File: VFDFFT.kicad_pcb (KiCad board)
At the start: 2 copper layers, 261 parts, among them J1 USB_C_Receptacle_USB2.0, J10 Conn_01x02_Pin, J11 Conn_01x02_Male, J12 Conn_01x02_Male, J13 Conn_01x02_Male, J2 BATT, J3 FILAMENT+, J4 VFD_SIG, J5 USB_A, J6 Conn_01x03_Socket, J7 Conn_01x03_Socket, J8 Conn_01x02_Pin, J9 Conn_01x02_Pin, Q1 IRL7486MTRPBF, Q10 AO3400A, Q11 AO3400A, Q12 FS5N10S, Q2 ASDM30DN40E, Q3 ASDM30DN40E, Q4 HSCB2903, Q5 HSCB2903, Q6 AP6800, Q7 FS5N10S, Q8 FS5N10S, Q9 AO3400A, U1 IP2368, U10 TPS61170, U11 TPS61170, U12 W25Q128JVS, U13 TPS62170DSG, U14 LM358, U15 LM324, U16 LM3478, U17 LM2738, U18 LTC1446, U2 78L05_SOT23, U3 TPS40305, U4 LM3478, U5 LM3478, U6 STM32F446VETx, U7 AP6181, U8 HDC1080, U9 OPT3001DNPR, X1 SX1M32.768KM10F30TNN, Y1 26M, Y2 24M

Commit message: file sync
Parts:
- Y1: value 26M -> WTL3M45404LZ; footprint Crystal:Crystal_SMD_2016-4Pin_2.0x1.6mm -> Crystal:Crystal_SMD_3225-4Pin_3.2x2.5mm
- moved U12 263.9 mm to (-174.3, 77.1)
- moved U10 239.1 mm to (-144.2, 46.5)
- moved D11 238.5 mm to (-148.4, 56.4)
- moved L9 236.9 mm to (-147.3, 28.2)
- moved L7 233.1 mm to (-147.7, 52.9)
- moved C68 229.2 mm to (-148.3, 46.2)
- moved C71 229.2 mm to (-148.3, 49.2)
- moved U9 229.1 mm to (-116.8, -21.2)
- moved R58 227.7 mm to (-177.5, 84.3)
- moved U11 220.6 mm to (-121.5, 27.7)
- moved D12 217.8 mm to (-125.7, 37.6)
- moved L8 213.1 mm to (-125.0, 34.1)
- moved C76 212.1 mm to (-177.5, 81.8)
- moved U8 211.6 mm to (-116.0, -25.3)
- moved C72 210.5 mm to (-125.6, 27.4)
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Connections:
- C10 pad 2: Net-(Q2B-D) -> Net-(Q2A-S)
- C13 pad 2: Net-(Q3B-D) -> Net-(Q3A-S)
- C48 pad 1: Net-(U7-XTAL_IN) -> Net-(C48-Pad1)
- L1 pad 1: Net-(Q2B-D) -> Net-(Q2A-S)
- L1 pad 2: Net-(Q3B-D) -> Net-(Q3A-S)
- Q2 pad 5: Net-(Q2B-D) -> Net-(Q2A-S)
- Q2 pad 7: Net-(Q2A-D)_1 -> Net-(U1-PCIN)
- Q2 pad 8: Net-(Q2A-D) -> Net-(U1-PCIN)
- Q3 pad 5: Net-(Q3B-D) -> Net-(Q3A-S)
- Q3 pad 7: Net-(Q3A-D)_1 -> Net-(U1-PCON)
- Q3 pad 8: Net-(Q3A-D) -> Net-(U1-PCON)
- R10 pad 1: Net-(Q2A-D) -> Net-(U1-PCIN)
- R11 pad 1: Net-(Q2B-D) -> Net-(Q2A-S)
- R12 pad 1: Net-(Q3A-D) -> Net-(U1-PCON)
- R13 pad 1: Net-(Q3A-D) -> Net-(U1-PCON)
- R14 pad 1: Net-(Q3B-D) -> Net-(Q3A-S)
- R42 pad 2: Net-(R42-Pad2) -> Net-(C48-Pad1)
- R9 pad 1: Net-(Q2A-D) -> Net-(U1-PCIN)
- U1 pad 15: Net-(Q2A-D)_1 -> Net-(U1-PCIN)
- U1 pad 18: Net-(Q2B-D) -> Net-(Q2A-S)
- U1 pad 21: Net-(Q3B-D) -> Net-(Q3A-S)
- U1 pad 24: Net-(Q3A-D)_1 -> Net-(U1-PCON)
- Y1 pad 2: Net-(R42-Pad2) -> GND
- Y1 pad 3: (no net) -> Net-(C48-Pad1)
- Y1 pad 4: (no net) -> GND
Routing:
- net GND: track 0.00 -> 133.0 mm, vias 0 -> 171
- net +BATT: track 0.00 -> 130.9 mm, vias 0 -> 17
- net /HLED: track 0.00 -> 79.7 mm, vias 0 -> 7
- net /CC2: track 0.00 -> 67.5 mm, vias 0 -> 2
- net PRI_HI: track 0.00 -> 61.0 mm, vias 0 -> 4
- net /BAT_MODE: track 0.00 -> 59.0 mm, vias 0 -> 6
- net /CC1: track 0.00 -> 57.7 mm, vias 0 -> 6
- net Net-(Q3A-G): track 0.00 -> 37.8 mm, vias 0 -> 2
- net Net-(D7-A2): track 0.00 -> 36.1 mm, vias 0 -> 2
- net Net-(Q3B-G): track 0.00 -> 36.0 mm, vias 0 -> 2
- net Net-(U1-PCON): track 0.00 -> 35.9 mm, vias 0 -> 17
- net /LED3: track 0.00 -> 31.5 mm, vias 0 -> 3
- net Net-(Q3A-S): track 0.00 -> 31.3 mm, vias 0 -> 62
- net /3V3_FB: track 0.00 -> 25.6 mm, vias 0 -> 4
- net +3V3: track 0.00 -> 24.8 mm, vias 0 -> 3
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- added copper zone on B.Cu, net +BATT
- added copper zone on F.Cu, net +BATT
- added copper zone on F.Cu, net /CC1
- added copper zone on F.Cu, net /CC2
- added copper zone on F.Cu, net /VB_S
- added copper zone on B.Cu, net GND
- added copper zone on F.Cu, net GND
- added copper zone on F.Cu, net Net-(F1-Pad1)
- added copper zone on F.Cu, net Net-(Q2A-S)
- added copper zone on B.Cu, net Net-(Q3A-S)
- added copper zone on F.Cu, net Net-(Q4A-D)
- added copper zone on F.Cu, net Net-(Q5A-D)
- added copper zone on B.Cu, net Net-(U1-PCIN)
- added copper zone on B.Cu, net Net-(U1-PCON)
- added copper zone on F.Cu, net VBUS
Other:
- board outline added: 100 x 50 mm
- board text added: "3V3"
- board text added: "ANODE BOOST"
- board text added: "BATTERY CHARGE"
- board text added: "Charging (NO DATA HERE)"
- board text added: "GRID BOOST"
- board text added: "SHELL MOS"
- board text added: "VDD VHP GND"
- board text added: "装不回去了吧"

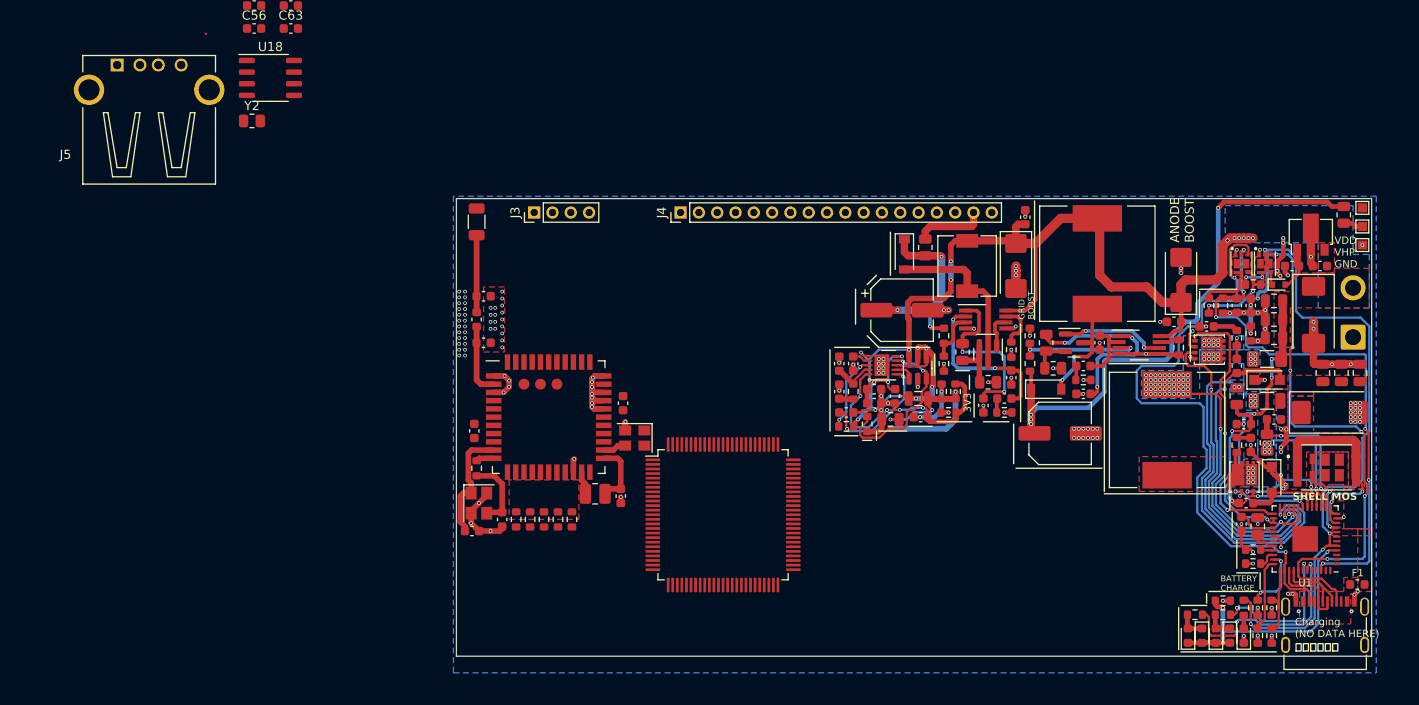
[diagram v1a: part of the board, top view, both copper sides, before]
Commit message: SDIO routing
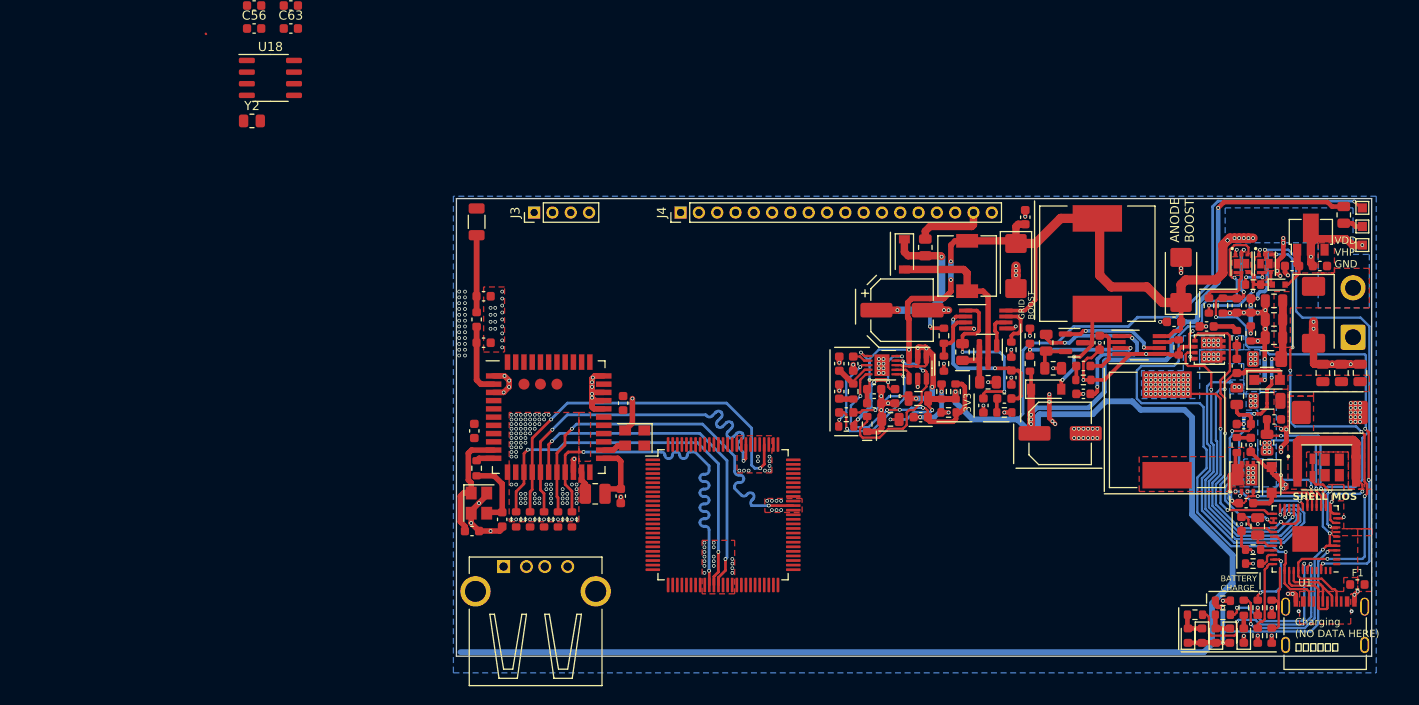
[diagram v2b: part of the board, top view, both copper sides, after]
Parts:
- moved J5 69.2 mm to (49.9, 77.0)
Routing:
- net +3V3: track 24.8 -> 212.8 mm, vias 3 -> 4
- net /WL_D2: track 0.00 -> 42.9 mm, vias 0 -> 2
- net /WL_D3: track 0.00 -> 42.7 mm, vias 0 -> 2
- net /WL_D1: track 0.00 -> 42.5 mm, vias 0 -> 2
- net /WL_D0: track 0.00 -> 42.4 mm, vias 0 -> 2
- net /WL_CMD: track 0.00 -> 41.8 mm, vias 0 -> 2
- net /WL_CLK: track 0.00 -> 38.2 mm, vias 0 -> 2
- net GND: track 133.0 -> 164.9 mm, vias 171 -> 305

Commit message: file sync
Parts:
- added C92: 1uF, Capacitor_SMD:C_0603_1608Metric, F.Cu at (24.0, 59.4)
- added C93: 1uF, Capacitor_SMD:C_0603_1608Metric, F.Cu at (24.0, 61.9)
- added C94: 1uF, Capacitor_SMD:C_0603_1608Metric, F.Cu at (24.0, 64.4)
- added C95: 10uF, Capacitor_SMD:C_0603_1608Metric, F.Cu at (24.0, 66.9)
- added C96: 4.7uF, Capacitor_SMD:C_0603_1608Metric, F.Cu at (-15.1, 65.6)
- added C97: 4.7uF, Capacitor_SMD:C_0603_1608Metric, F.Cu at (-15.1, 68.2)
- added C98: 3.3nF, Capacitor_SMD:C_0603_1608Metric, F.Cu at (109.5, 75.7)
- added J14: AudioJack3_Ground, Footprints:TRRS-PJ-320A, F.Cu at (-9.50, 67.0)
- added J15: USB_C_Receptacle_USB2.0, Footprints:TYPE-C-31-M-31, F.Cu at (114.8, 79.8)
- added R90: 100K, Capacitor_SMD:C_0603_1608Metric, F.Cu at (24.0, 69.5)
- added R91: 100K, Capacitor_SMD:C_0603_1608Metric, F.Cu at (24.0, 72.0)
- added R92: 1K, Resistor_SMD:R_0603_1608Metric, F.Cu at (80.8, 65.8)
- added R93: 1K, Resistor_SMD:R_0603_1608Metric, F.Cu at (109.5, 74.2)
- added R94: 5K1, Resistor_SMD:R_0603_1608Metric, F.Cu at (109.0, 82.3)
- added R95: 5K1, Resistor_SMD:R_0603_1608Metric, F.Cu at (121.7, 77.7)
- added RN2: 22, Resistor_SMD:R_Array_Concave_4x0603, F.Cu at (91.2, 76.2)
- added U19: CH340E, Package_SO:MSOP-10_3x3mm_P0.5mm, F.Cu at (114.3, 74.7)
- U18: value LTC1446 -> ES9023; footprint Package_SO:SO-8_3.9x4.9mm_P1.27mm -> Package_SO:SO-16_3.9x9.9mm_P1.27mm
- moved U12 262.0 mm to (87.6, 81.0), turned to 180 degrees
- moved C76 237.9 mm to (58.6, 111.4)
- moved R58 237.9 mm to (58.6, 114.0)
- moved R43 219.4 mm to (70.4, 81.8), turned to 90 degrees
- moved R44 214.6 mm to (67.8, 79.0), turned to 180 degrees
- moved U8 212.4 mm to (67.4, 81.9)
- moved R49 210.9 mm to (64.5, 82.3), turned to -90 degrees
- moved R47 210.7 mm to (63.0, 82.3), turned to 90 degrees
- moved U9 205.1 mm to (60.3, 82.3)
- moved RN1 187.6 mm to (73.7, 80.0), turned to 90 degrees
- moved R48 182.5 mm to (71.1, 38.4)
- moved C67 179.4 mm to (68.1, 38.4)
- moved U18 56.5 mm to (5.33, 75.2), turned to 90 degrees
- moved C56 18.2 mm to (16.3, 33.5)
- moved C63 18.2 mm to (20.3, 33.5)
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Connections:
- net Net-(J5-D+) renamed /D+
- net Net-(J5-D-) renamed /D-
- U18 pad 1: Net-(U18-SCK) -> Net-(RN2C-R3.1)
- U18 pad 2: Net-(U18-SDI) -> Net-(RN2B-R2.1)
- U18 pad 3: Net-(U18-~{CS}/LD) -> Net-(RN2A-R1.1)
- U18 pad 4: Net-(U18-SDO) -> GND
- U18 pad 5: /L -> +3V3
- U18 pad 6: GND -> Net-(U18-VREG)
- U18 pad 7: +5V -> /AUX_L
- U18 pad 8: /R -> /AUX_R
- U6 pad 15: /VFD_CS -> unconnected-(U6-PC0-Pad15)
- U6 pad 16: /VFD_DATA -> /AUX_I2S_SD
- U6 pad 29: /DAC1 -> /L
- U6 pad 30: /DAC2 -> /R
- U6 pad 43: Net-(U18-SCK) -> /VFD_CLK
- U6 pad 44: Net-(U18-SDO) -> /VFD_CS
- U6 pad 45: Net-(U18-SDI) -> /VFD_DATA
- U6 pad 46: Net-(U18-~{CS}/LD) -> /VFD_RST
- U6 pad 51: /VFD_RST -> /AUX_I2S_WS
- U6 pad 52: /VFD_CLK -> /AUX_I2S_CK
- U6 pad 63: unconnected-(U6-PC6-Pad63) -> /AUX_MCK
- U6 pad 68: unconnected-(U6-PA9-Pad68) -> Net-(U6-PA9)
- U6 pad 69: unconnected-(U6-PA10-Pad69) -> Net-(U6-PA10)
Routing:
- net +3V3: track 212.8 -> 410.8 mm, vias 4 -> 25
- net Net-(J4-Pin_9): track 0.00 -> 57.4 mm, vias 0 -> 1
- net Net-(J4-Pin_8): track 0.00 -> 57.1 mm, vias 0 -> 1
- net Net-(J4-Pin_7): track 0.00 -> 57.1 mm, vias 0 -> 1
- net Net-(J4-Pin_6): track 0.00 -> 57.0 mm, vias 0 -> 1
- net /FLASH_IO2: track 0.00 -> 52.3 mm, vias 0 -> 4
- net /D-: track 0.00 -> 43.4 mm, vias 0 -> 1
- net /D+: track 0.00 -> 43.3 mm, vias 0 -> 1
- net /FLASH_SCK: track 0.00 -> 39.3 mm, vias 0 -> 2
- net GND: track 164.9 -> 201.5 mm, vias 305 -> 354
- net /OPT_SDA: track 0.00 -> 34.9 mm, vias 0 -> 4
- net Net-(U6-PA10): track 0.00 -> 34.8 mm
- net Net-(U19-RXD): track 0.00 -> 34.4 mm
- net /FLASH_IO3: track 0.00 -> 31.2 mm, vias 0 -> 2
- net /FLASH_IO1: track 0.00 -> 30.0 mm
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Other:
- board text added: "DATA (NO Charging HERE)"

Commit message: file sync
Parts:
- C65, C66: value 10nF -> ??
- Y2: footprint Resistor_SMD:R_0805_2012Metric -> Crystal:Crystal_SMD_3225-4Pin_3.2x2.5mm
- moved C87 189.0 mm to (85.6, 48.8), turned to 90 degrees
- moved R82 187.2 mm to (85.6, 43.4), turned to -90 degrees
- moved C83 182.8 mm to (79.7, 38.9)
- moved C84 182.7 mm to (79.8, 40.4)
- moved C85 180.8 mm to (82.8, 45.2), turned to -90 degrees
- moved U16 179.8 mm to (84.8, 39.4)
- moved R81 179.0 mm to (77.5, 39.7), turned to 90 degrees
- moved C86 177.5 mm to (75.2, 39.1), turned to 180 degrees
- moved R86 175.9 mm to (75.2, 40.6)
- moved L10 174.2 mm to (77.5, 45.2), turned to -90 degrees
- moved R85 170.7 mm to (69.6, 40.9), turned to -90 degrees
- moved Q12 162.5 mm to (72.1, 47.0), turned to -90 degrees
- moved D14 161.7 mm to (71.6, 43.7)
- moved R83 161.5 mm to (72.1, 41.4), turned to 180 degrees
- moved R84 159.1 mm to (69.3, 46.7), turned to -90 degrees
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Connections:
- Y2 pad 2: Net-(U6-PH0) -> GND
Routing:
- net /FLASH_CS: track 0.00 -> 69.8 mm, vias 0 -> 2
- net /HUM_SCK: track 1.55 -> 43.0 mm, vias 0 -> 6
- net /HUM_SDA: track 2.72 -> 38.5 mm, vias 0 -> 4
- net +BATT: track 130.9 -> 157.1 mm, vias 17 -> 22
- net GND: track 201.5 -> 226.6 mm, vias 354 -> 368
- net Net-(Q12-G): track 0.00 -> 21.5 mm, vias 0 -> 2
- net /AUX_I2S_SD: track 13.5 -> 34.0 mm, vias 1 -> 4
- net /FB_15: track 0.00 -> 18.8 mm, vias 0 -> 2
- net /ISEN_15: track 0.00 -> 12.1 mm
- net Net-(U6-PH0): track 0.00 -> 9.61 mm
- net Net-(U16-FA/SD): track 0.00 -> 8.79 mm
- net Net-(U6-PH1): track 0.00 -> 7.93 mm
- net Net-(Q12-S): track 0.00 -> 6.60 mm
- net Net-(D14-A): track 0.00 -> 5.08 mm
- net +3V3: track 410.8 -> 415.5 mm, vias 25 -> 28
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- added copper zone on F.Cu, net Net-(D14-A)

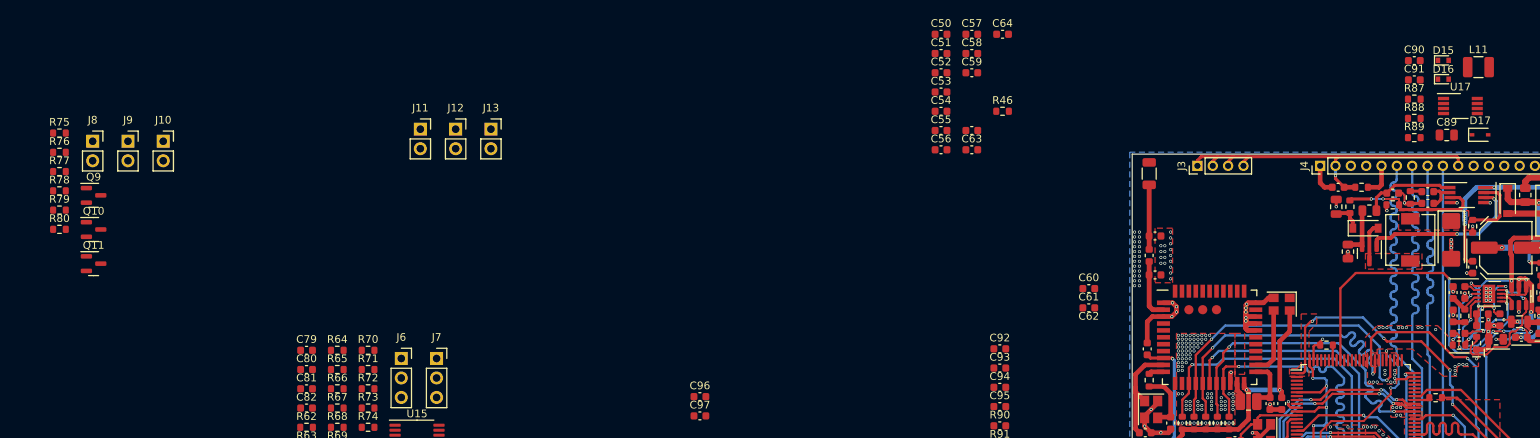
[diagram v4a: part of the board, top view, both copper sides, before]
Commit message: Laser ON/OFF
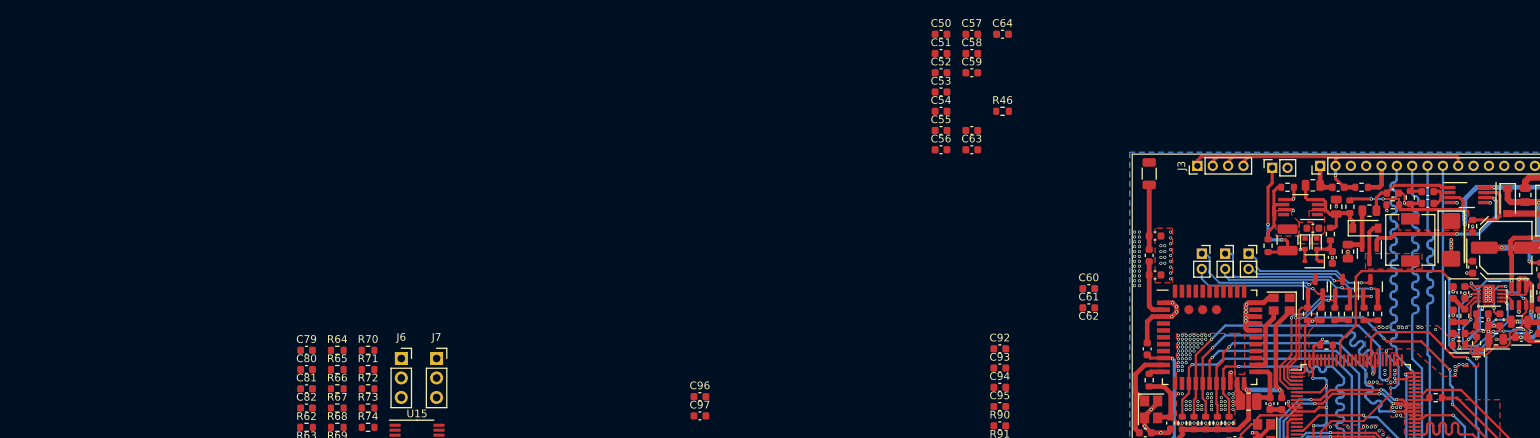
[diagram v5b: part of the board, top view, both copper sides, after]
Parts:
- removed J12, J13: Conn_01x02_Male, Connector_PinSocket_2.54mm:PinSocket_1x02_P2.54mm_Vertical
- J10, J11, J8, J9: footprint Connector_PinSocket_2.54mm:PinSocket_1x02_P2.54mm_Vertical -> Connector_PinSocket_2.00mm:PinSocket_1x02_P2.00mm_Vertical
- moved R80 172.2 mm to (73.2, 54.9), turned to 90 degrees
- moved R79 170.6 mm to (71.4, 54.9), turned to 90 degrees
- moved R78 168.8 mm to (69.4, 54.9), turned to 90 degrees
- moved R77 167.3 mm to (67.6, 54.9), turned to 90 degrees
- moved Q11 166.5 mm to (72.3, 51.3), turned to 90 degrees
- moved R75 166.1 mm to (65.9, 54.9), turned to 90 degrees
- moved R76 164.0 mm to (64.1, 54.9), turned to 90 degrees
- moved Q10 163.0 mm to (68.6, 51.3), turned to 90 degrees
- moved Q9 159.7 mm to (65.1, 51.3), turned to 90 degrees
- moved J8 145.3 mm to (50.3, 47.0)
- moved J9 143.8 mm to (53.3, 47.0)
- moved J10 142.2 mm to (56.4, 47.0)
- moved J11 111.2 mm to (59.5, 35.8), turned to 90 degrees
- moved L11 33.6 mm to (61.5, 45.2), turned to -90 degrees
- moved D15 29.9 mm to (63.8, 45.7), turned to -90 degrees
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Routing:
- net /LB: track 0.00 -> 26.0 mm, vias 0 -> 2
- net Net-(J9-Pin_2): track 0.00 -> 20.2 mm, vias 0 -> 1
- net Net-(J10-Pin_2): track 0.00 -> 20.1 mm, vias 0 -> 1
- net Net-(J8-Pin_2): track 0.00 -> 19.7 mm, vias 0 -> 1
- net /LG: track 0.00 -> 18.5 mm, vias 0 -> 2
- net Net-(J9-Pin_1): track 0.00 -> 18.3 mm, vias 0 -> 1
- net Net-(J10-Pin_1): track 0.00 -> 18.2 mm, vias 0 -> 1
- net Net-(J8-Pin_1): track 0.00 -> 18.0 mm, vias 0 -> 1
- net +12V: track 0.00 -> 15.9 mm, vias 0 -> 2
- net /LR: track 0.00 -> 13.9 mm
- net +15V: track 3.96 -> 15.6 mm
- net Net-(U17-FB): track 0.00 -> 10.2 mm
- net GND: track 226.6 -> 233.8 mm, vias 368 -> 372
- net Net-(D16-A): track 0.00 -> 6.32 mm
- net Net-(R79-Pad1): track 0.00 -> 1.78 mm
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- added copper zone on F.Cu, net Net-(D15-K)
- added copper zone on F.Cu, net Net-(D16-K)

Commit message: file sync
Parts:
- J6, J7: footprint Connector_PinSocket_2.54mm:PinSocket_1x03_P2.54mm_Vertical -> Connector_PinSocket_2.00mm:PinSocket_1x03_P2.00mm_Vertical
- moved C70 269.6 mm to (116.1, 71.9), turned to 180 degrees
- moved R52 266.4 mm to (113.0, 71.9), turned to 180 degrees
- moved C68 265.8 mm to (116.6, 68.1), turned to -90 degrees
- moved U10 264.2 mm to (119.1, 68.4)
- moved C69 263.8 mm to (110.0, 71.9), turned to 180 degrees
- moved R54 262.3 mm to (109.5, 69.6), turned to 90 degrees
- moved L7 262.0 mm to (113.8, 68.7), turned to -90 degrees
- moved R53 261.7 mm to (109.0, 65.3), turned to -90 degrees
- moved D11 260.0 mm to (111.3, 69.3), turned to 90 degrees
- moved C71 259.5 mm to (110.7, 65.5), turned to 90 degrees
- moved C74 259.2 mm to (125.5, 74.2), turned to 90 degrees
- moved R56 256.8 mm to (124.0, 74.2), turned to -90 degrees
- moved R57 255.0 mm to (122.4, 74.7), turned to 90 degrees
- moved R55 254.3 mm to (120.9, 74.7), turned to 90 degrees
- moved C73 252.1 mm to (118.4, 71.4), turned to -90 degrees
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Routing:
- net +BATT: track 157.1 -> 250.3 mm, vias 22 -> 30
- net GNDA: track 0.00 -> 74.5 mm, vias 0 -> 9
- net Net-(R75-Pad1): track 1.78 -> 54.1 mm, vias 0 -> 4
- net /FLASH_IO2: track 52.3 -> 0.00 mm, vias 4 -> 0
- net +5V: track 0.00 -> 48.9 mm, vias 0 -> 3
- net VDDA: track 0.00 -> 46.1 mm, vias 0 -> 5
- net /L: track 0.00 -> 43.2 mm, vias 0 -> 4
- net Net-(U6-PA10): track 34.8 -> 1.95 mm
- net Net-(U19-RXD): track 34.4 -> 3.93 mm
- net /L-: track 0.00 -> 25.9 mm, vias 0 -> 1
- net +3V3: track 415.9 -> 441.5 mm, vias 28 -> 29
- net GND: track 233.8 -> 259.1 mm, vias 372 -> 371
- net /L+: track 0.00 -> 24.7 mm, vias 0 -> 3
- net Net-(U15C--): track 0.00 -> 21.3 mm, vias 0 -> 2
- net Net-(U10-FB): track 0.00 -> 18.9 mm, vias 0 -> 2
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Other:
- board text added: "BATT CHARGE"
- board text removed: "BATTERY CHARGE"
